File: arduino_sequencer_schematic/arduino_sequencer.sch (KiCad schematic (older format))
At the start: 174 parts, among them J1 AudioJack, J10 AudioJack, J11 AudioJack, J12 AudioJack, J13 AudioJack, J14 AudioJack, J15 AudioJack, J16 Conn_02x05, J2 AudioJack, J3 AudioJack, J4 AudioJack, J5 AudioJack, J6 AudioJack, J7 AudioJack, J8 AudioJack, J9 AudioJack, Q1 2N3904, Q10 2N3904, Q11 2N3904, Q2 2N3904, Q3 2N3904, Q4 2N3904, Q5 2N3904, Q6 2N3904, Q7 2N3904, Q8 2N3904, Q9 2N3904, SW1 SW_SPST, SW2 SW_Push, SW3 SW_Push, SW4 SW_Push, SW5 SW_SPST, SW6 SW_SPST, U1 74HC595, U2 TL084, U3 TL084, U4 L7805

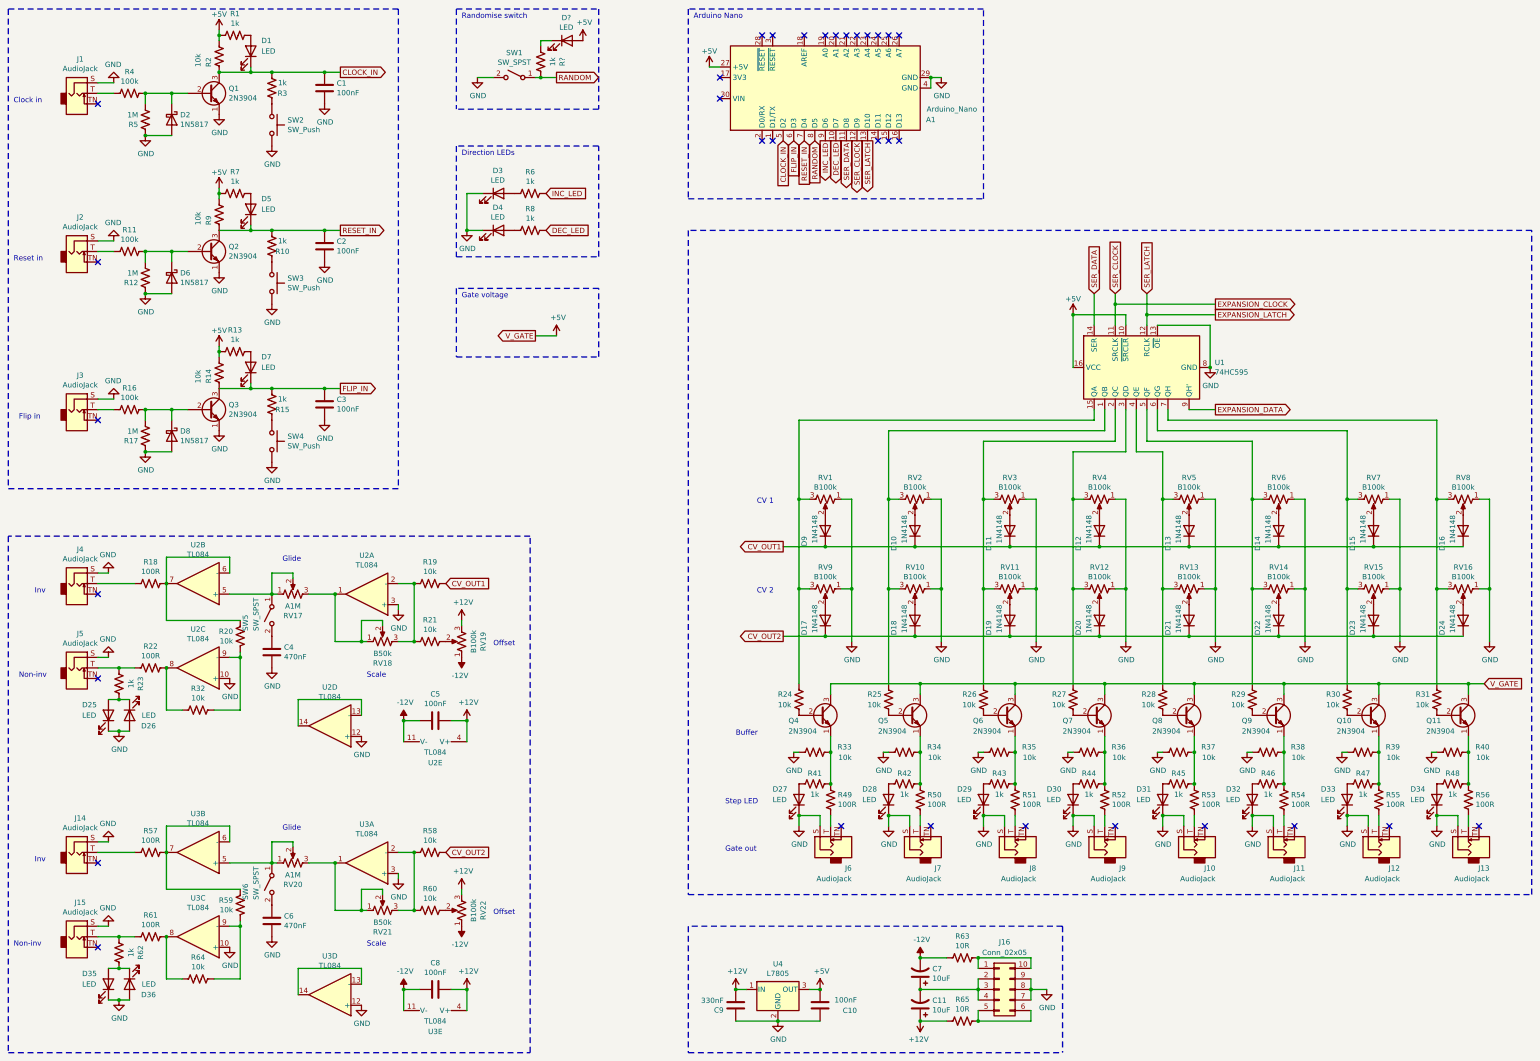
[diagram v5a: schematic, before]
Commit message: Added footprints
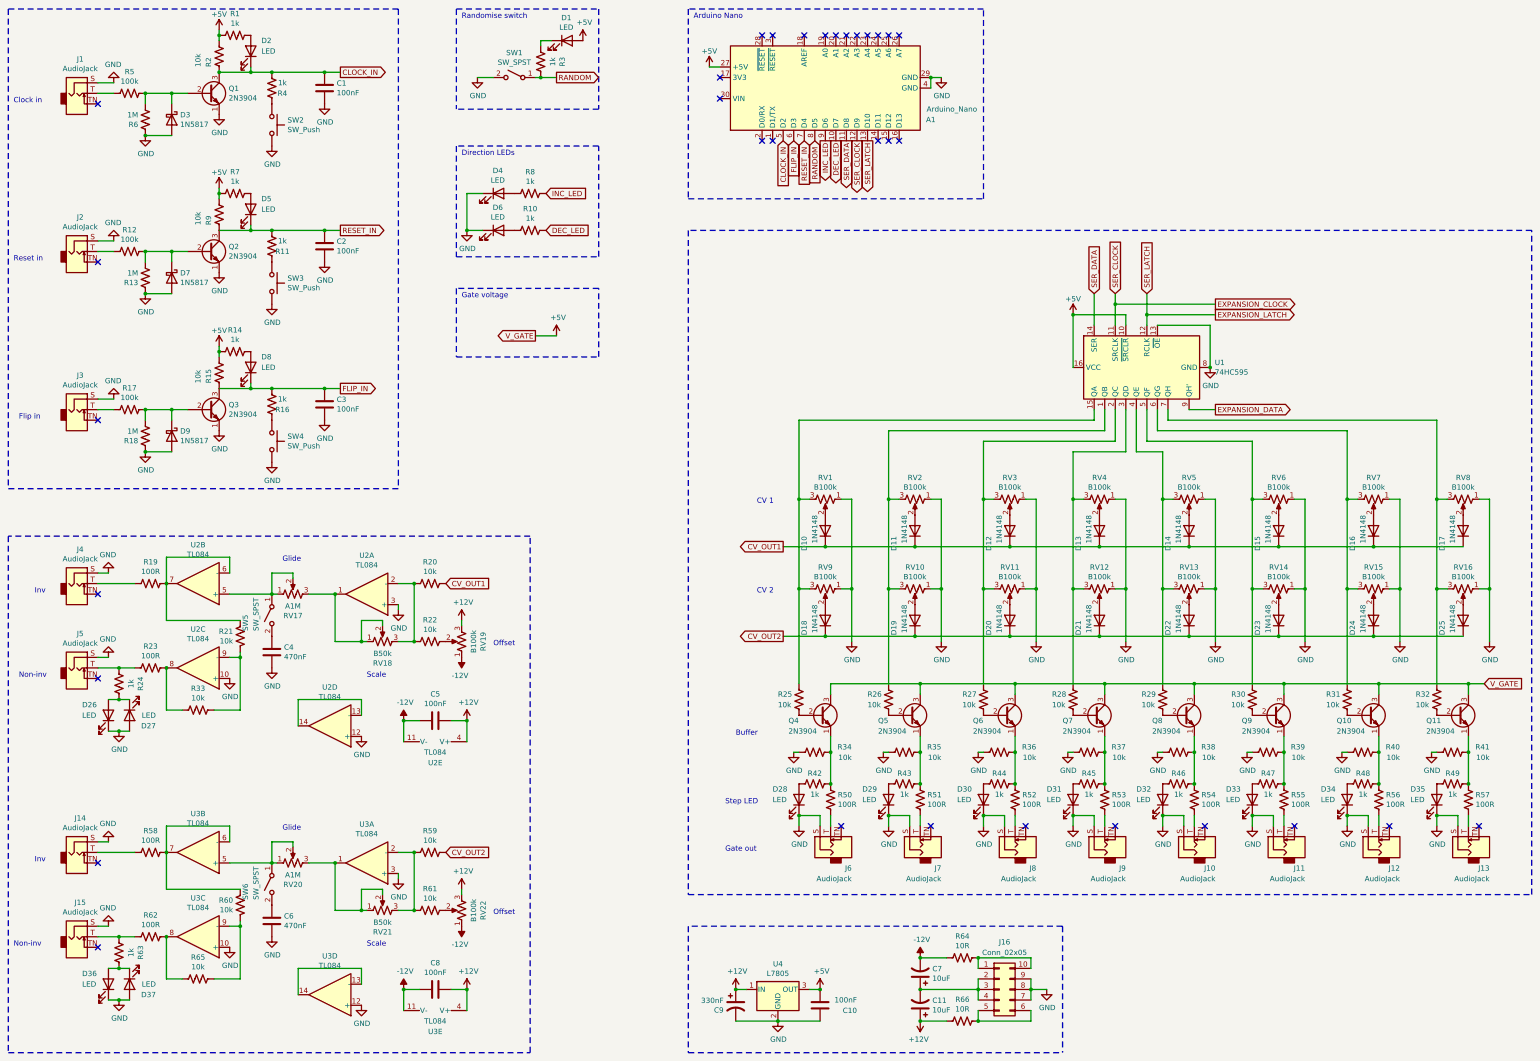
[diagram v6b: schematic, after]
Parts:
- removed C9: 330nF, symbol Device:C
- added C9: 330nF, Capacitor_THT:CP_Radial_D10.0mm_P3.80mm, symbol Device:CP1
- C1, C10, C2, C3, C5, C8: footprint (none) -> Capacitor_THT:C_Disc_D6.0mm_W2.5mm_P5.00mm
- C11, C7: footprint (none) -> Capacitor_THT:CP_Radial_D10.0mm_P3.80mm
- C4, C6: footprint (none) -> Capacitor_THT:C_Disc_D14.5mm_W5.0mm_P7.50mm
- D1: renamed from D?; footprint (none) -> LED_THT:LED_D5.0mm
- D2: renamed from D1; footprint (none) -> LED_THT:LED_D5.0mm
- D26: renamed from D25; footprint (none) -> LED_THT:LED_D5.0mm
- D27: renamed from D26; footprint (none) -> LED_THT:LED_D5.0mm
- D28: renamed from D27; footprint (none) -> LED_THT:LED_D5.0mm
- D29: renamed from D28; footprint (none) -> LED_THT:LED_D5.0mm
- D30: renamed from D29; footprint (none) -> LED_THT:LED_D5.0mm
- D31: renamed from D30; footprint (none) -> LED_THT:LED_D5.0mm
- D32: renamed from D31; footprint (none) -> LED_THT:LED_D5.0mm
- D33: renamed from D32; footprint (none) -> LED_THT:LED_D5.0mm
- D34: renamed from D33; footprint (none) -> LED_THT:LED_D5.0mm
- D35: renamed from D34; footprint (none) -> LED_THT:LED_D5.0mm
- D36: renamed from D35; footprint (none) -> LED_THT:LED_D5.0mm
- D37: renamed from D36; footprint (none) -> LED_THT:LED_D5.0mm
- D4: renamed from D3; footprint (none) -> LED_THT:LED_D5.0mm
- D5: footprint (none) -> LED_THT:LED_D5.0mm
- D6: renamed from D4; footprint (none) -> LED_THT:LED_D5.0mm
- D8: renamed from D7; footprint (none) -> LED_THT:LED_D5.0mm
- J1, J10, J11, J12, J13, J14, J15, J2, J3, J4, J5, J6, J7, J8, J9: footprint (none) -> Connector_JST:JST_EH_B2B-EH-A_1x02_P2.50mm_Vertical
- J16: footprint (none) -> Connector_IDC:IDC-Header_2x05_P2.54mm_Vertical
- R1, R2, R7, R9: footprint (none) -> Resistor_THT:R_Axial_DIN0207_L6.3mm_D2.5mm_P10.16mm_Horizontal
- R10: renamed from R8; footprint (none) -> Resistor_THT:R_Axial_DIN0207_L6.3mm_D2.5mm_P10.16mm_Horizontal
- R11: renamed from R10; footprint (none) -> Resistor_THT:R_Axial_DIN0207_L6.3mm_D2.5mm_P10.16mm_Horizontal
- R12: renamed from R11; footprint (none) -> Resistor_THT:R_Axial_DIN0207_L6.3mm_D2.5mm_P10.16mm_Horizontal
- R13: renamed from R12; footprint (none) -> Resistor_THT:R_Axial_DIN0207_L6.3mm_D2.5mm_P10.16mm_Horizontal
- R14: renamed from R13; footprint (none) -> Resistor_THT:R_Axial_DIN0207_L6.3mm_D2.5mm_P10.16mm_Horizontal
- R15: renamed from R14; footprint (none) -> Resistor_THT:R_Axial_DIN0207_L6.3mm_D2.5mm_P10.16mm_Horizontal
- R16: renamed from R15; footprint (none) -> Resistor_THT:R_Axial_DIN0207_L6.3mm_D2.5mm_P10.16mm_Horizontal
- R17: renamed from R16; footprint (none) -> Resistor_THT:R_Axial_DIN0207_L6.3mm_D2.5mm_P10.16mm_Horizontal
- R18: renamed from R17; footprint (none) -> Resistor_THT:R_Axial_DIN0207_L6.3mm_D2.5mm_P10.16mm_Horizontal
- R19: renamed from R18; footprint (none) -> Resistor_THT:R_Axial_DIN0207_L6.3mm_D2.5mm_P10.16mm_Horizontal
- R20: renamed from R19; footprint (none) -> Resistor_THT:R_Axial_DIN0207_L6.3mm_D2.5mm_P10.16mm_Horizontal
- R21: renamed from R20; footprint (none) -> Resistor_THT:R_Axial_DIN0207_L6.3mm_D2.5mm_P10.16mm_Horizontal
- R22: renamed from R21; footprint (none) -> Resistor_THT:R_Axial_DIN0207_L6.3mm_D2.5mm_P10.16mm_Horizontal
- R23: renamed from R22; footprint (none) -> Resistor_THT:R_Axial_DIN0207_L6.3mm_D2.5mm_P10.16mm_Horizontal
- R24: renamed from R23; footprint (none) -> Resistor_THT:R_Axial_DIN0207_L6.3mm_D2.5mm_P10.16mm_Horizontal
- R25: renamed from R24; footprint (none) -> Resistor_THT:R_Axial_DIN0207_L6.3mm_D2.5mm_P10.16mm_Horizontal
- R26: renamed from R25; footprint (none) -> Resistor_THT:R_Axial_DIN0207_L6.3mm_D2.5mm_P10.16mm_Horizontal
- R27: renamed from R26; footprint (none) -> Resistor_THT:R_Axial_DIN0207_L6.3mm_D2.5mm_P10.16mm_Horizontal
- R28: renamed from R27; footprint (none) -> Resistor_THT:R_Axial_DIN0207_L6.3mm_D2.5mm_P10.16mm_Horizontal
- R29: renamed from R28; footprint (none) -> Resistor_THT:R_Axial_DIN0207_L6.3mm_D2.5mm_P10.16mm_Horizontal
- R3: renamed from R?; footprint (none) -> Resistor_THT:R_Axial_DIN0207_L6.3mm_D2.5mm_P10.16mm_Horizontal
- R30: renamed from R29; footprint (none) -> Resistor_THT:R_Axial_DIN0207_L6.3mm_D2.5mm_P10.16mm_Horizontal
- R31: renamed from R30; footprint (none) -> Resistor_THT:R_Axial_DIN0207_L6.3mm_D2.5mm_P10.16mm_Horizontal
- R32: renamed from R31; footprint (none) -> Resistor_THT:R_Axial_DIN0207_L6.3mm_D2.5mm_P10.16mm_Horizontal
- R33: renamed from R32; footprint (none) -> Resistor_THT:R_Axial_DIN0207_L6.3mm_D2.5mm_P10.16mm_Horizontal
- R34: renamed from R33; footprint (none) -> Resistor_THT:R_Axial_DIN0207_L6.3mm_D2.5mm_P10.16mm_Horizontal
- R35: renamed from R34; footprint (none) -> Resistor_THT:R_Axial_DIN0207_L6.3mm_D2.5mm_P10.16mm_Horizontal
- R36: renamed from R35; footprint (none) -> Resistor_THT:R_Axial_DIN0207_L6.3mm_D2.5mm_P10.16mm_Horizontal
- R37: renamed from R36; footprint (none) -> Resistor_THT:R_Axial_DIN0207_L6.3mm_D2.5mm_P10.16mm_Horizontal
- R38: renamed from R37; footprint (none) -> Resistor_THT:R_Axial_DIN0207_L6.3mm_D2.5mm_P10.16mm_Horizontal
- R39: renamed from R38; footprint (none) -> Resistor_THT:R_Axial_DIN0207_L6.3mm_D2.5mm_P10.16mm_Horizontal
- R4: renamed from R3; footprint (none) -> Resistor_THT:R_Axial_DIN0207_L6.3mm_D2.5mm_P10.16mm_Horizontal
- R40: renamed from R39; footprint (none) -> Resistor_THT:R_Axial_DIN0207_L6.3mm_D2.5mm_P10.16mm_Horizontal
- R41: renamed from R40; footprint (none) -> Resistor_THT:R_Axial_DIN0207_L6.3mm_D2.5mm_P10.16mm_Horizontal
- R42: renamed from R41; footprint (none) -> Resistor_THT:R_Axial_DIN0207_L6.3mm_D2.5mm_P10.16mm_Horizontal
- R43: renamed from R42; footprint (none) -> Resistor_THT:R_Axial_DIN0207_L6.3mm_D2.5mm_P10.16mm_Horizontal
- R44: renamed from R43; footprint (none) -> Resistor_THT:R_Axial_DIN0207_L6.3mm_D2.5mm_P10.16mm_Horizontal
- R45: renamed from R44; footprint (none) -> Resistor_THT:R_Axial_DIN0207_L6.3mm_D2.5mm_P10.16mm_Horizontal
- R46: renamed from R45; footprint (none) -> Resistor_THT:R_Axial_DIN0207_L6.3mm_D2.5mm_P10.16mm_Horizontal
- R47: renamed from R46; footprint (none) -> Resistor_THT:R_Axial_DIN0207_L6.3mm_D2.5mm_P10.16mm_Horizontal
- R48: renamed from R47; footprint (none) -> Resistor_THT:R_Axial_DIN0207_L6.3mm_D2.5mm_P10.16mm_Horizontal
- R49: renamed from R48; footprint (none) -> Resistor_THT:R_Axial_DIN0207_L6.3mm_D2.5mm_P10.16mm_Horizontal
- R5: renamed from R4; footprint (none) -> Resistor_THT:R_Axial_DIN0207_L6.3mm_D2.5mm_P10.16mm_Horizontal
- R50: renamed from R49; footprint (none) -> Resistor_THT:R_Axial_DIN0207_L6.3mm_D2.5mm_P10.16mm_Horizontal
- R51: renamed from R50; footprint (none) -> Resistor_THT:R_Axial_DIN0207_L6.3mm_D2.5mm_P10.16mm_Horizontal
- R52: renamed from R51; footprint (none) -> Resistor_THT:R_Axial_DIN0207_L6.3mm_D2.5mm_P10.16mm_Horizontal
- R53: renamed from R52; footprint (none) -> Resistor_THT:R_Axial_DIN0207_L6.3mm_D2.5mm_P10.16mm_Horizontal
- R54: renamed from R53; footprint (none) -> Resistor_THT:R_Axial_DIN0207_L6.3mm_D2.5mm_P10.16mm_Horizontal
- R55: renamed from R54; footprint (none) -> Resistor_THT:R_Axial_DIN0207_L6.3mm_D2.5mm_P10.16mm_Horizontal
- R56: renamed from R55; footprint (none) -> Resistor_THT:R_Axial_DIN0207_L6.3mm_D2.5mm_P10.16mm_Horizontal
- R57: renamed from R56; footprint (none) -> Resistor_THT:R_Axial_DIN0207_L6.3mm_D2.5mm_P10.16mm_Horizontal
- R58: renamed from R57; footprint (none) -> Resistor_THT:R_Axial_DIN0207_L6.3mm_D2.5mm_P10.16mm_Horizontal
- R59: renamed from R58; footprint (none) -> Resistor_THT:R_Axial_DIN0207_L6.3mm_D2.5mm_P10.16mm_Horizontal
- R6: renamed from R5; footprint (none) -> Resistor_THT:R_Axial_DIN0207_L6.3mm_D2.5mm_P10.16mm_Horizontal
- R60: renamed from R59; footprint (none) -> Resistor_THT:R_Axial_DIN0207_L6.3mm_D2.5mm_P10.16mm_Horizontal
- R61: renamed from R60; footprint (none) -> Resistor_THT:R_Axial_DIN0207_L6.3mm_D2.5mm_P10.16mm_Horizontal
- R62: renamed from R61; footprint (none) -> Resistor_THT:R_Axial_DIN0207_L6.3mm_D2.5mm_P10.16mm_Horizontal
- R63: renamed from R62; footprint (none) -> Resistor_THT:R_Axial_DIN0207_L6.3mm_D2.5mm_P10.16mm_Horizontal
- R64: renamed from R63; footprint (none) -> Resistor_THT:R_Axial_DIN0207_L6.3mm_D2.5mm_P10.16mm_Horizontal
- R65: renamed from R64; footprint (none) -> Resistor_THT:R_Axial_DIN0207_L6.3mm_D2.5mm_P10.16mm_Horizontal
- R66: renamed from R65; footprint (none) -> Resistor_THT:R_Axial_DIN0207_L6.3mm_D2.5mm_P10.16mm_Horizontal
- R8: renamed from R6; footprint (none) -> Resistor_THT:R_Axial_DIN0207_L6.3mm_D2.5mm_P10.16mm_Horizontal
- RV1, RV10, RV11, RV12, RV13, RV14, RV15, RV16, RV17, RV18, RV19, RV2, RV20, RV21, RV22, RV3, RV4, RV5, RV6, RV7, RV8, RV9: footprint (none) -> Potentiometer_THT:Potentiometer_Alpha_RD901F-40-00D_Single_Vertical
- SW1, SW5, SW6: footprint (none) -> TimMJN:Switch_SP
- SW2, SW3, SW4: footprint (none) -> TimMJN:Mom_push_button
- U1: footprint (none) -> Package_DIP:DIP-16_W7.62mm
- U2, U3: footprint (none) -> Package_DIP:DIP-14_W7.62mm
- U4: footprint (none) -> Package_TO_SOT_THT:TO-220-3_Vertical
- renumbered D9 to D10, D10 to D11, D11 to D12, D12 to D13, D13 to D14, D14 to D15, D15 to D16, D16 to D17, D17 to D18, D18 to D19, D19 to D20, D20 to D21, D21 to D22, D22 to D23, D23 to D24, D24 to D25, D2 to D3, D6 to D7, D8 to D9
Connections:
- net +12V: now also C9.1
- net GND: now also C9.2
